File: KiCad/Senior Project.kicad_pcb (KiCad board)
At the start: 4 copper layers, 59.2 x 89.2 mm, 48 parts, among them J2 Screw_Terminal_01x02, J3 Screw_Terminal_01x06, J4 Conn_ARM_JTAG_SWD_10, J5 Conn_01x03, J6 Conn_01x02, J7 USB4105-GF-A, Q2 IRLML0030, Q3 IRLML0030, Q4 IRLML0030, SW1 SW_Push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

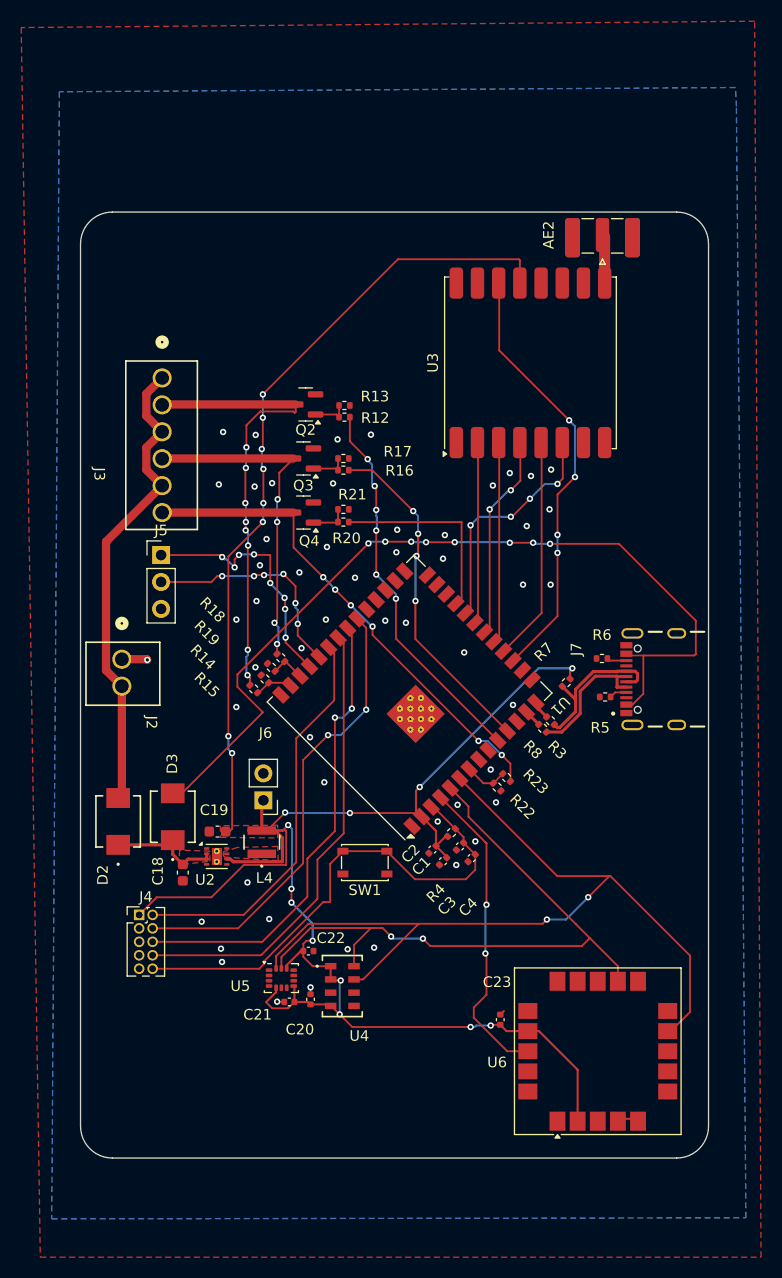
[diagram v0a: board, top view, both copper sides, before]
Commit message: Major routing changes, back copper now 3V3 instead of ground, utilized back traces more.
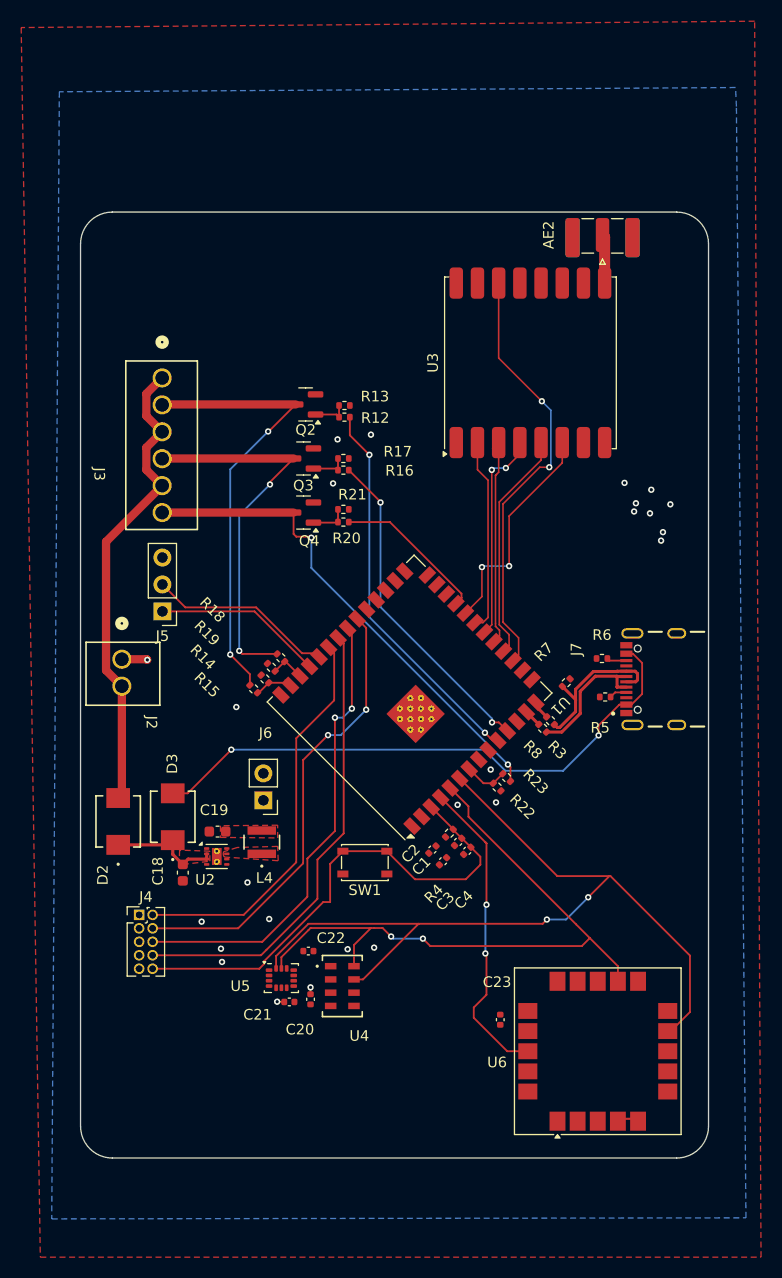
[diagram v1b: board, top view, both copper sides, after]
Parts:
- moved J5 5.32 mm to (131.7, 87.4), turned to 180 degrees
- moved C4 0.80 mm to (160.5, 110.0)
- moved C3 0.46 mm to (159.6, 109.2)
- moved R4 0.21 mm to (158.8, 108.3)
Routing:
- net +3V3: track 226.5 -> 0.00 mm, vias 20 -> 0
- net Net-(D3-A): track 83.5 -> 55.1 mm, vias 8 -> 2
- net /UOTXD: track 23.8 -> 16.0 mm, vias 8 -> 0
- net /Pyro Channel2/Pyro Pin: track 31.8 -> 36.4 mm, vias 4 -> 2
- net /UORXD: track 21.1 -> 17.6 mm, vias 6 -> 0
- net /Pyro GPIO 3: track 18.6 -> 15.3 mm
- net /FSPIQ: track 16.7 -> 18.8 mm
- net /FSPID: track 18.5 -> 20.4 mm
- net /FSPICLK: track 19.0 -> 20.6 mm
- net /FSPICS0: track 20.7 -> 21.9 mm
- net /Pyro GPIO 2: track 32.3 -> 31.2 mm, vias 4 -> 2
- net /Pyro Channel1/Pyro Pin: track 43.5 -> 42.5 mm, vias 8 -> 2
- net /EN: track 46.8 -> 47.3 mm
- net GND: track 6.68 -> 6.20 mm, vias 53 -> 25
- net /Interrupt: track 40.6 -> 40.9 mm, vias 4 -> 2
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- added copper zone on B.Cu, net +3V3
- removed copper zone on B.Cu, net GND

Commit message: fixed all drc errors, adjusted routing and added ground plane
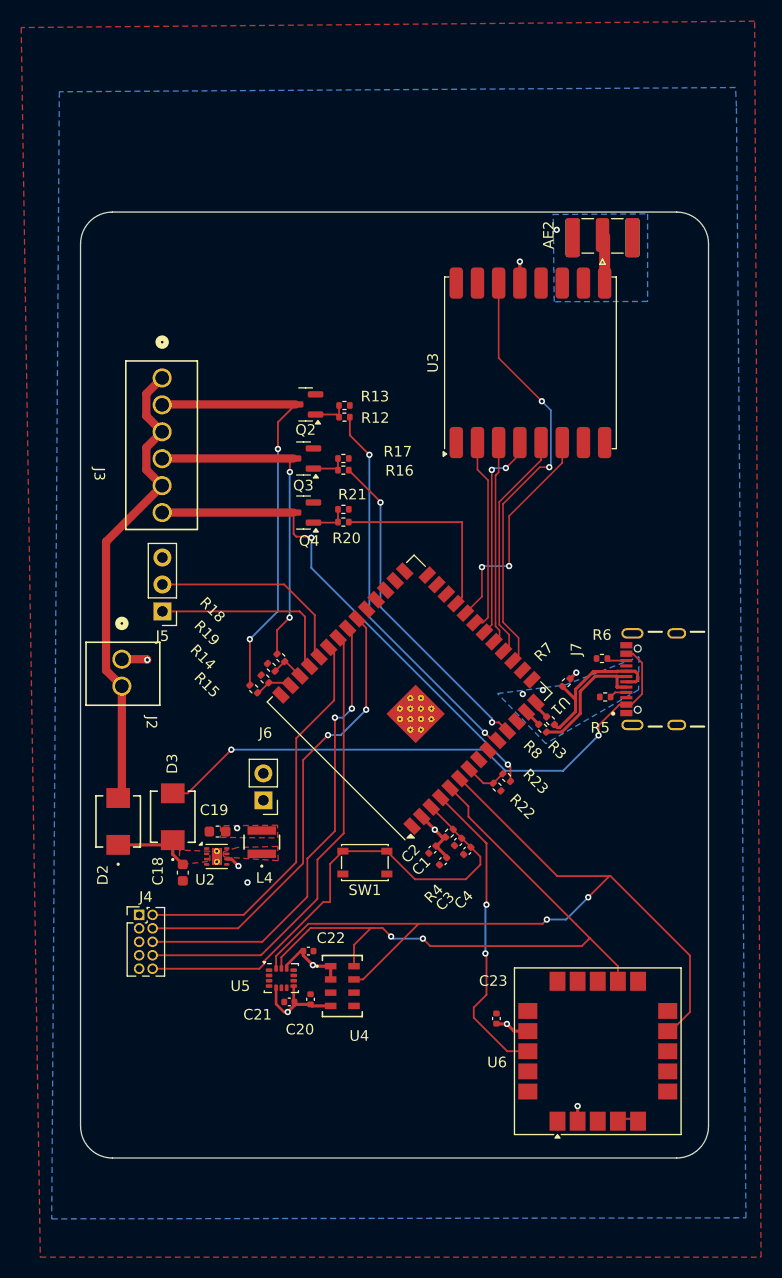
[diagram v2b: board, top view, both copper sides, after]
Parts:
- moved C23 0.38 mm to (163.2, 125.8)
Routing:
- net +3V3: track 0.00 -> 31.3 mm, vias 0 -> 9
- net /Pyro Channel2/Pyro Pin: track 36.4 -> 31.5 mm
- net /Pyro GPIO 3: track 15.3 -> 18.6 mm
- net +VDC: track 11.0 -> 8.02 mm
- net /UOTXD: track 16.0 -> 18.5 mm
- net /UORXD: track 17.6 -> 19.7 mm
- net /Pyro Channel1/Pyro Pin: track 42.5 -> 40.9 mm
- net GND: track 6.20 -> 4.87 mm, vias 25 -> 5
- added copper zone on B.Cu, net GND

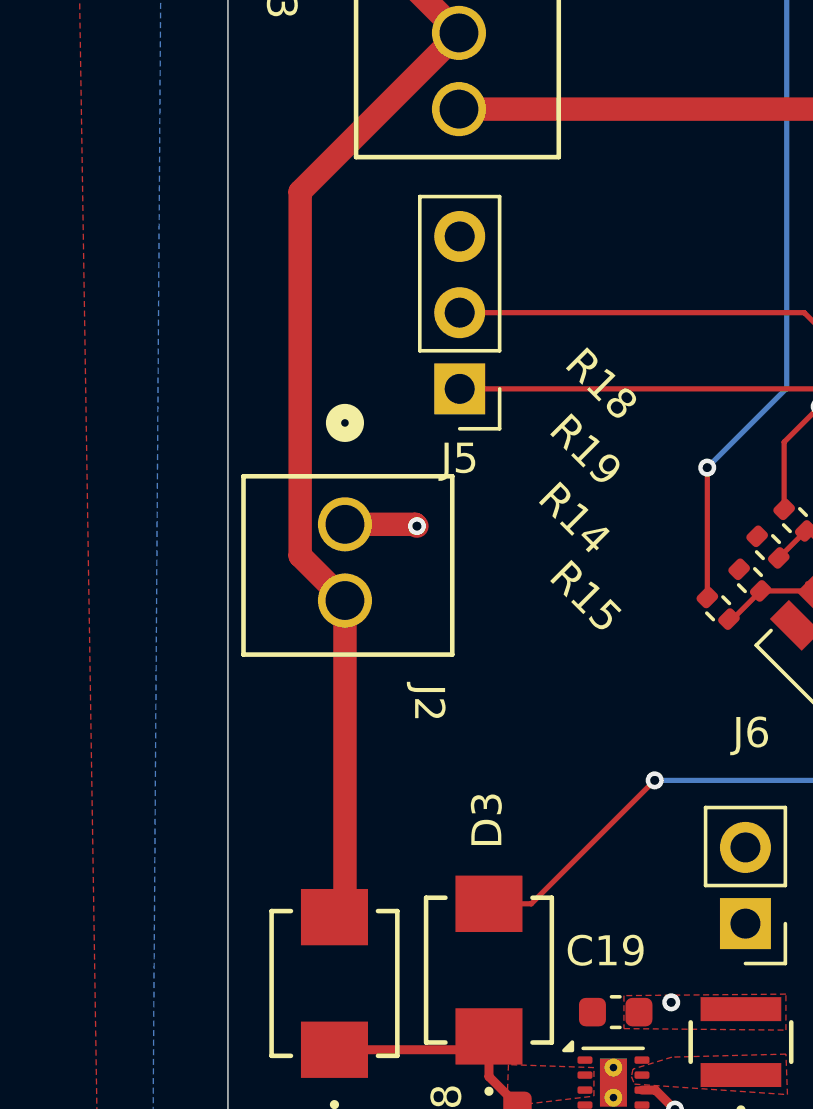
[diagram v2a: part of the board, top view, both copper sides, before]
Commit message: Barometer schematic fix, JST connector, and few other fixes
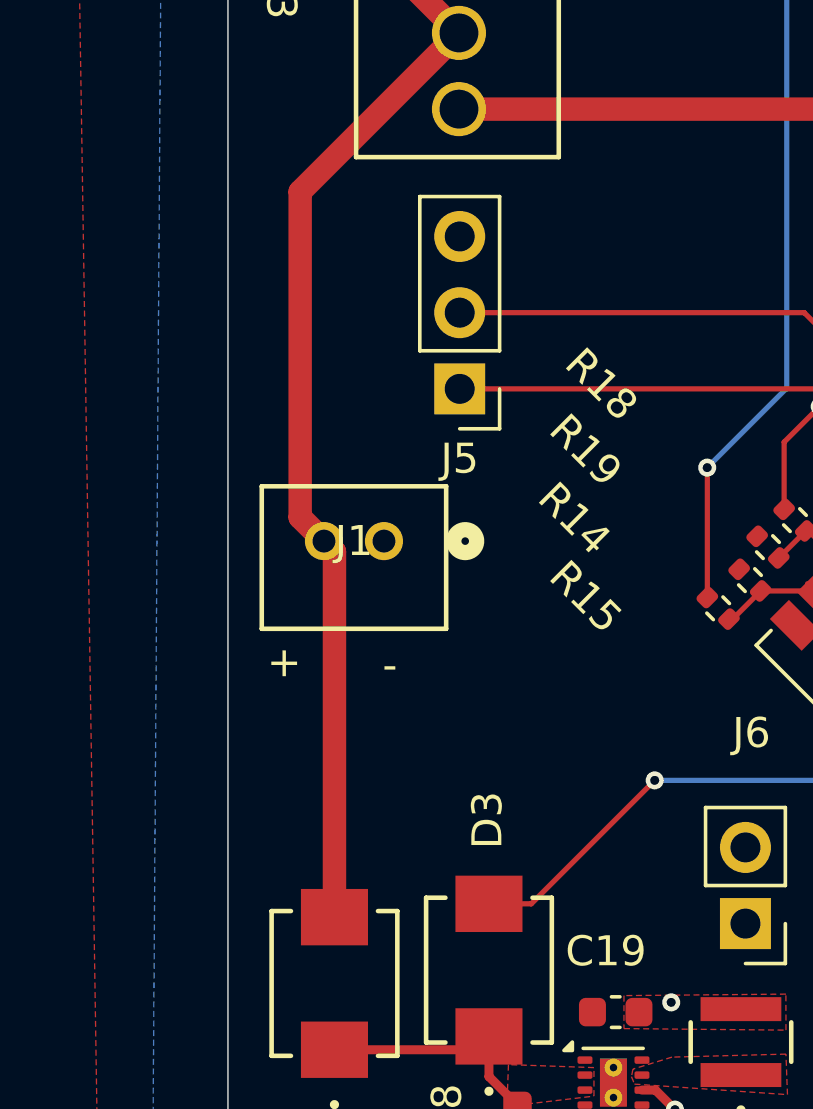
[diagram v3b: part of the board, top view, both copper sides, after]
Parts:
- removed J2: Screw_Terminal_01x02, OSTVN02A150:CONN_OSTVN02A150_OST
- added J1: B2B-PH-K-S, footprints:CONN2_B2B-PH-K-S_JST, F.Cu at (129.2, 92.5)
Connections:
- U4 pad 5: GND -> unconnected-(U4-~{CSB__1}-Pad5)
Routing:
- net GND: track 4.87 -> 2.45 mm, vias 5 -> 4
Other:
- board text added: "+"
- board text added: "-"

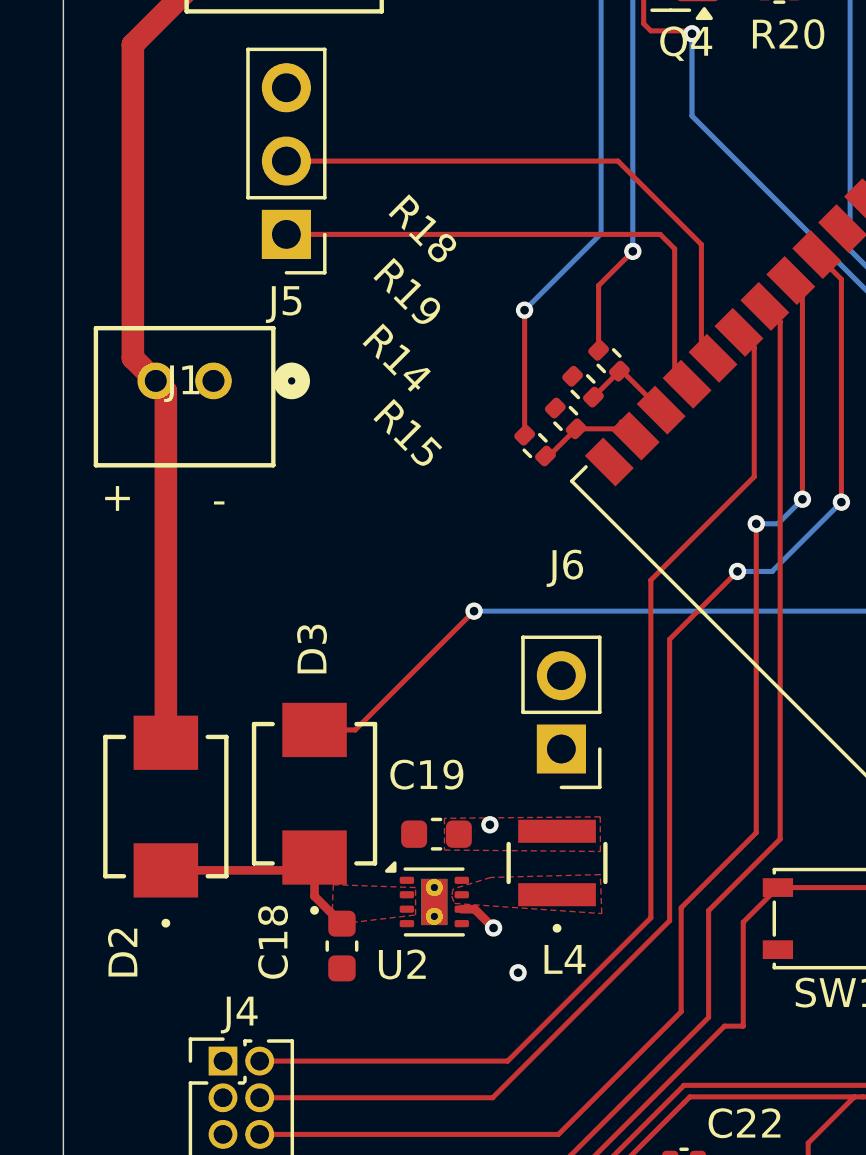
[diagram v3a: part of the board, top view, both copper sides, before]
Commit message: Back silkscreen text added
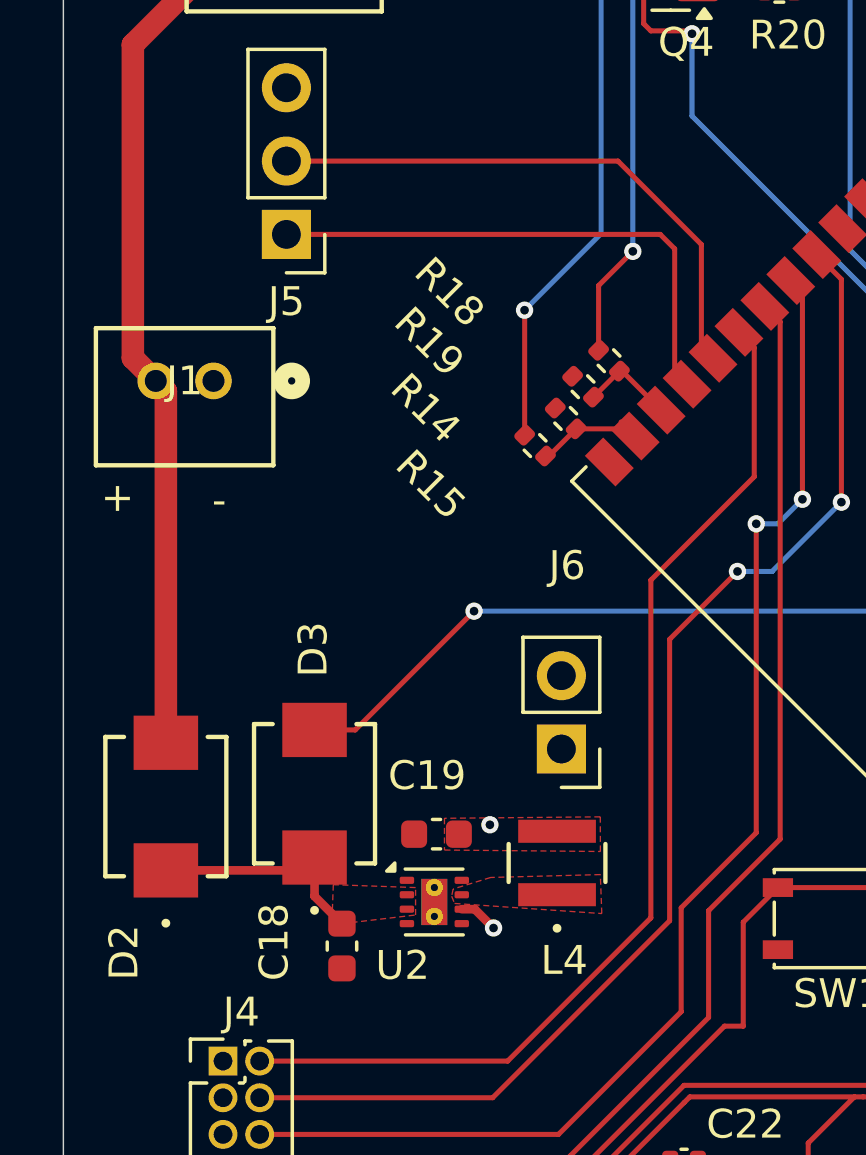
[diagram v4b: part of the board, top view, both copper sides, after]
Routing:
- net GND: vias 4 -> 3
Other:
- board text added: "OSU Chapter of AIAA Avionics System Design Team 2025"
- board text added: "Senior Design Group 15 2025 Designed by: Anthony Rubio Devasis Aryal Alexander Nutt Abdulrahman Almutairi"
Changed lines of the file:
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@@
 		(tags "resistor")
 		(property "Reference" "R19"
-			(at 6.576093 -2.015254 135)
+			(at 4.861359 -2.669328 135)
 			(layer "F.SilkS")
 			(effects
@@
 		(tags "resistor")
 		(property "Reference" "R15"
-			(at 3.473991 -4.268828 135)
+			(at 1.679379 -4.93207 135)
 			(layer "F.SilkS")
 			(effects
@@
 		(tags "resistor")
 		(property "Reference" "R14"
-			(at -5.500408 1.272792 135)
+			(at -3.59122 1.767767 135)
 			(layer "F.SilkS")
 			(effects
@@
 		(tags "resistor")
 		(property "Reference" "R18"
-			(at -7.760497 1.361181 135)
+			(at -5.586144 2.227386 135)
 			(layer "F.SilkS")
 			(effects
@@
 		)
 	)
+	(gr_text "Senior Design Group 15 2025\nDesigned by: \nAnthony Rubio\nDevasis Aryal\nAlexander Nutt\nAbdulrahman Almutairi"
+		(at 151.875 61.025 0)
+		(layer "B.SilkS")
+		(effects
+			(font
+				(size 1 1)
+				(thickness 0.15)
+			)
+			(justify left bottom mirror)
+		)
+	)
+	(gr_text "OSU Chapter of AIAA\nAvionics System Design Team 2025"
+		(at 155.75 134.8 0)
+		(layer "B.SilkS")
+		(effects
+			(font
+				(size 1 1)
+				(thickness 0.15)
+			)
+			(justify left bottom mirror)
+		)
+	)
 	(segment
 		(start 174.7 135.3)
@@
 		(size 0.6)
 		(drill 0.3)
-		(layers "F.Cu" "B.Cu")
-		(free yes)
-		(net 1)
-	)
-	(via
-		(at 139.75 113)
-		(size 0.6)
-		(drill 0.3)

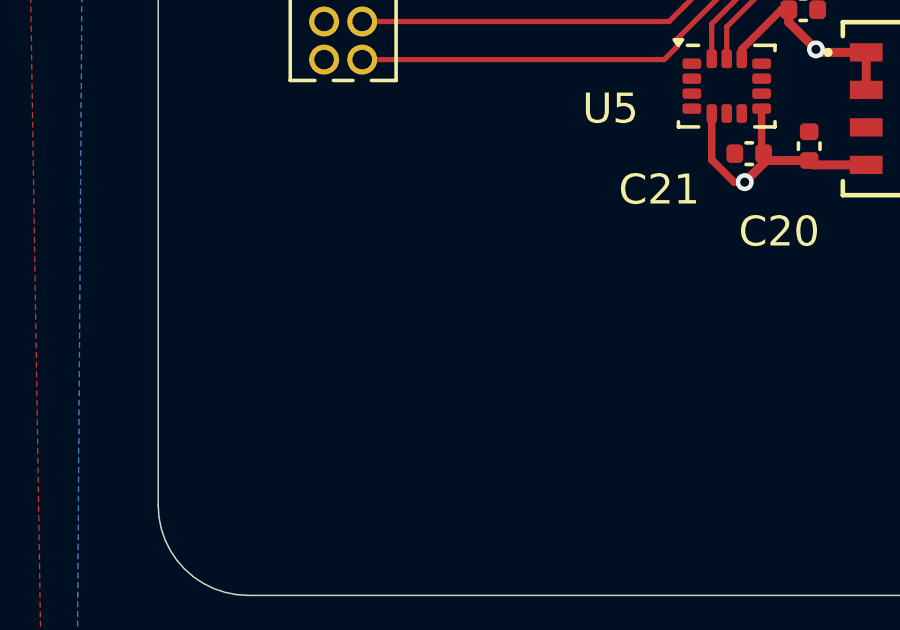
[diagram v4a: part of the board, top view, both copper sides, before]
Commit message: Switch added, LCSC table, other changes.
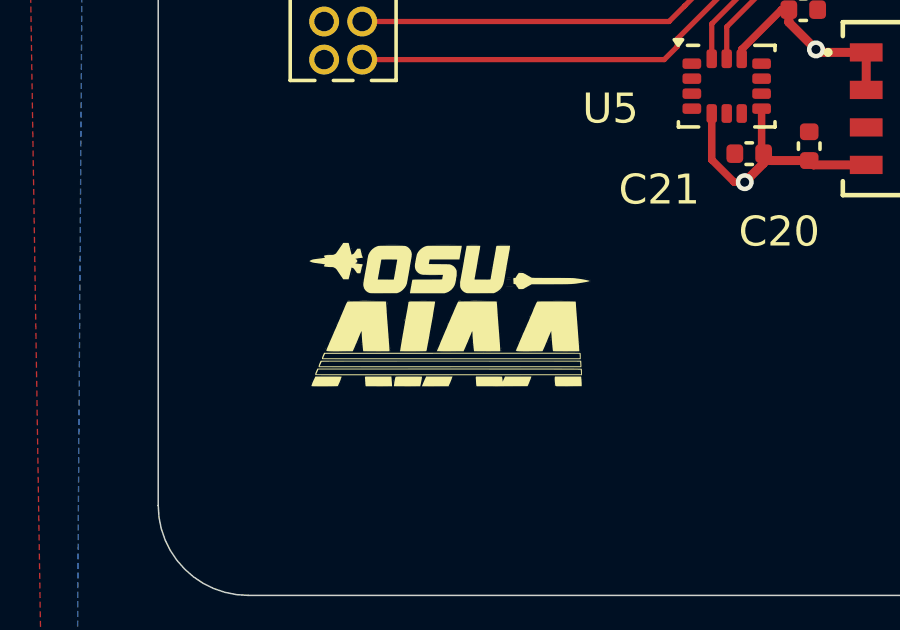
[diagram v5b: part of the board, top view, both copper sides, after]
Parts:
- added G***: LOGO, JST_Connector:test_logo, F.Cu at (133.7, 129.7)
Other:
- copper layers 4 -> 2
- board text added: "With help from: Max Leibowitz Joe Fitzpatrick"
